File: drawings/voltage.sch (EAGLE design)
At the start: 6 parts, among them U1 THS4532IPW, U2 MAX9944ATA+T

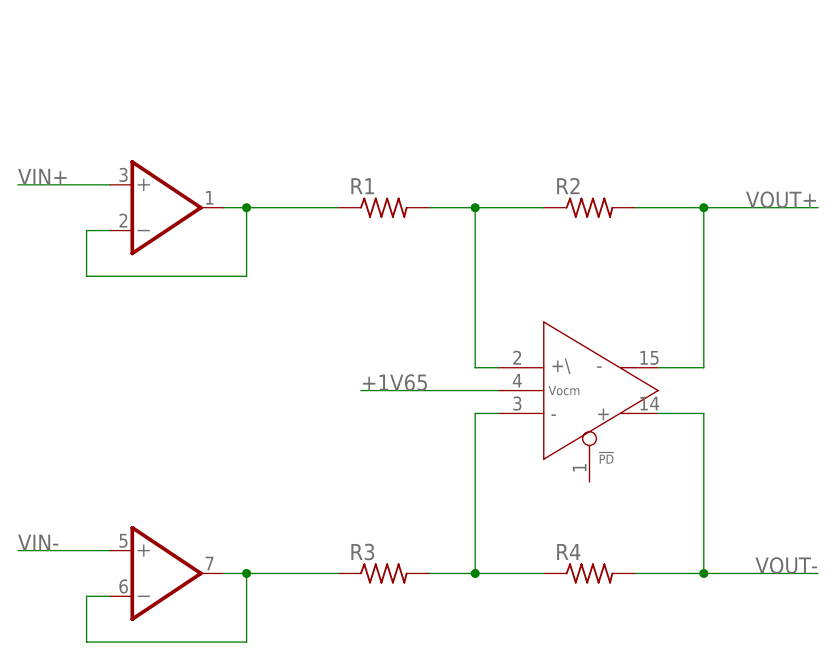
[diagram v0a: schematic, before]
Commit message: Updated drawings of voltage and current circuits
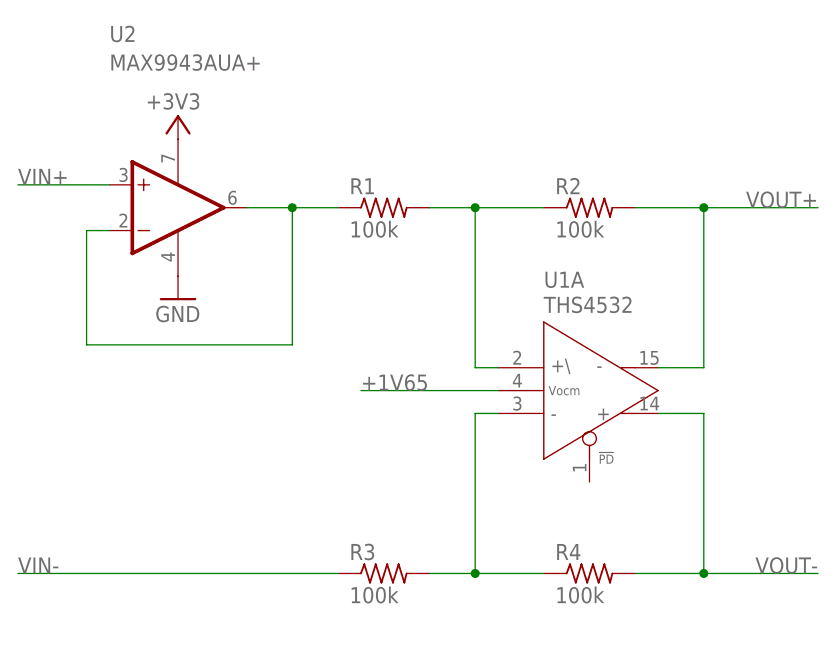
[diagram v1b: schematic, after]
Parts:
- R1, R2, R3, R4: value (none) -> 100k
- U1: value THS4532IPW -> THS4532; device Soil Power Sensor:THS4532IPW -> Soil Power Sensor:THS4532
- U2: value MAX9944ATA+T -> MAX9943AUA+; device Soil Power Sensor:MAX9944ATA+T -> Soil Power Sensor:MAX9943AUA+
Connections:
- removed net N$4: R3.1, U2B.-IN, U2B.OUT
- new net +3V3: U2.V+
- new net GND: U2.V-
- net N$2: now also U2.-IN, U2.OUT; no longer U2A.-IN, U2A.OUT
- net VIN+: now also U2.+IN; no longer U2A.+IN
- net VIN-: now also R3.1; no longer U2B.+IN
